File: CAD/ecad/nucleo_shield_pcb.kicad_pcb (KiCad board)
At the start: 2 copper layers, 70 x 57 mm, 6 parts, among them J1 CN7, J2 CN10

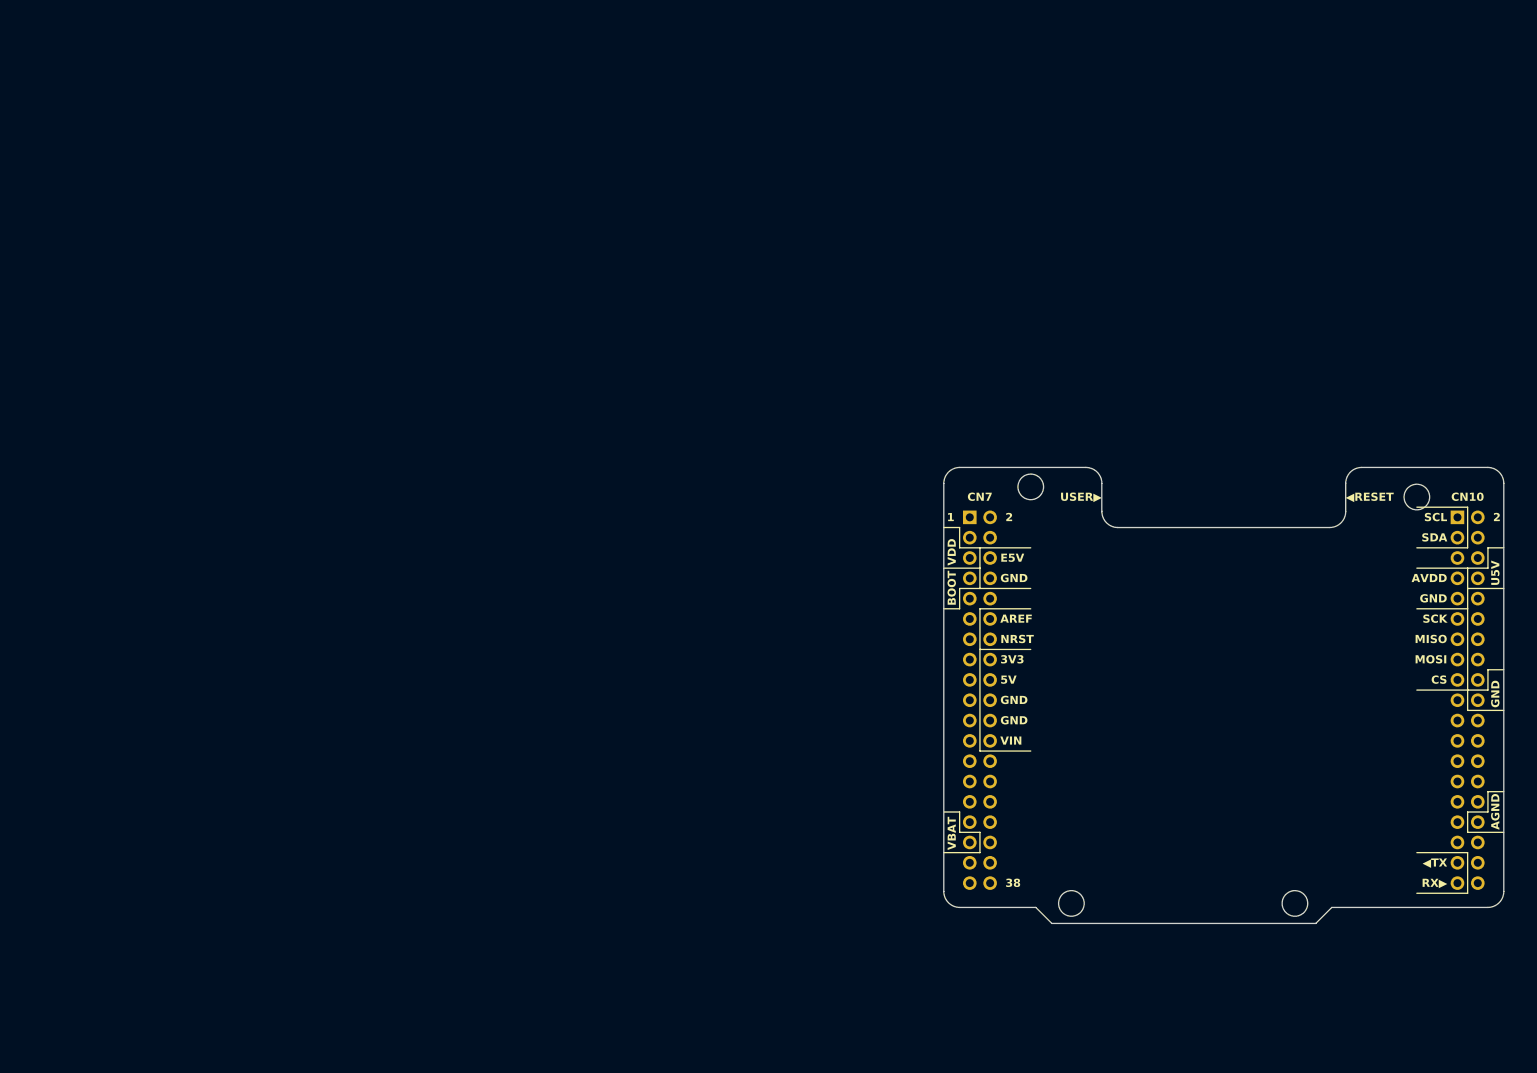
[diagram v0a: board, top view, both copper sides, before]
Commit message: Update KiCad schematic and layout with new ESP32 button circuitry
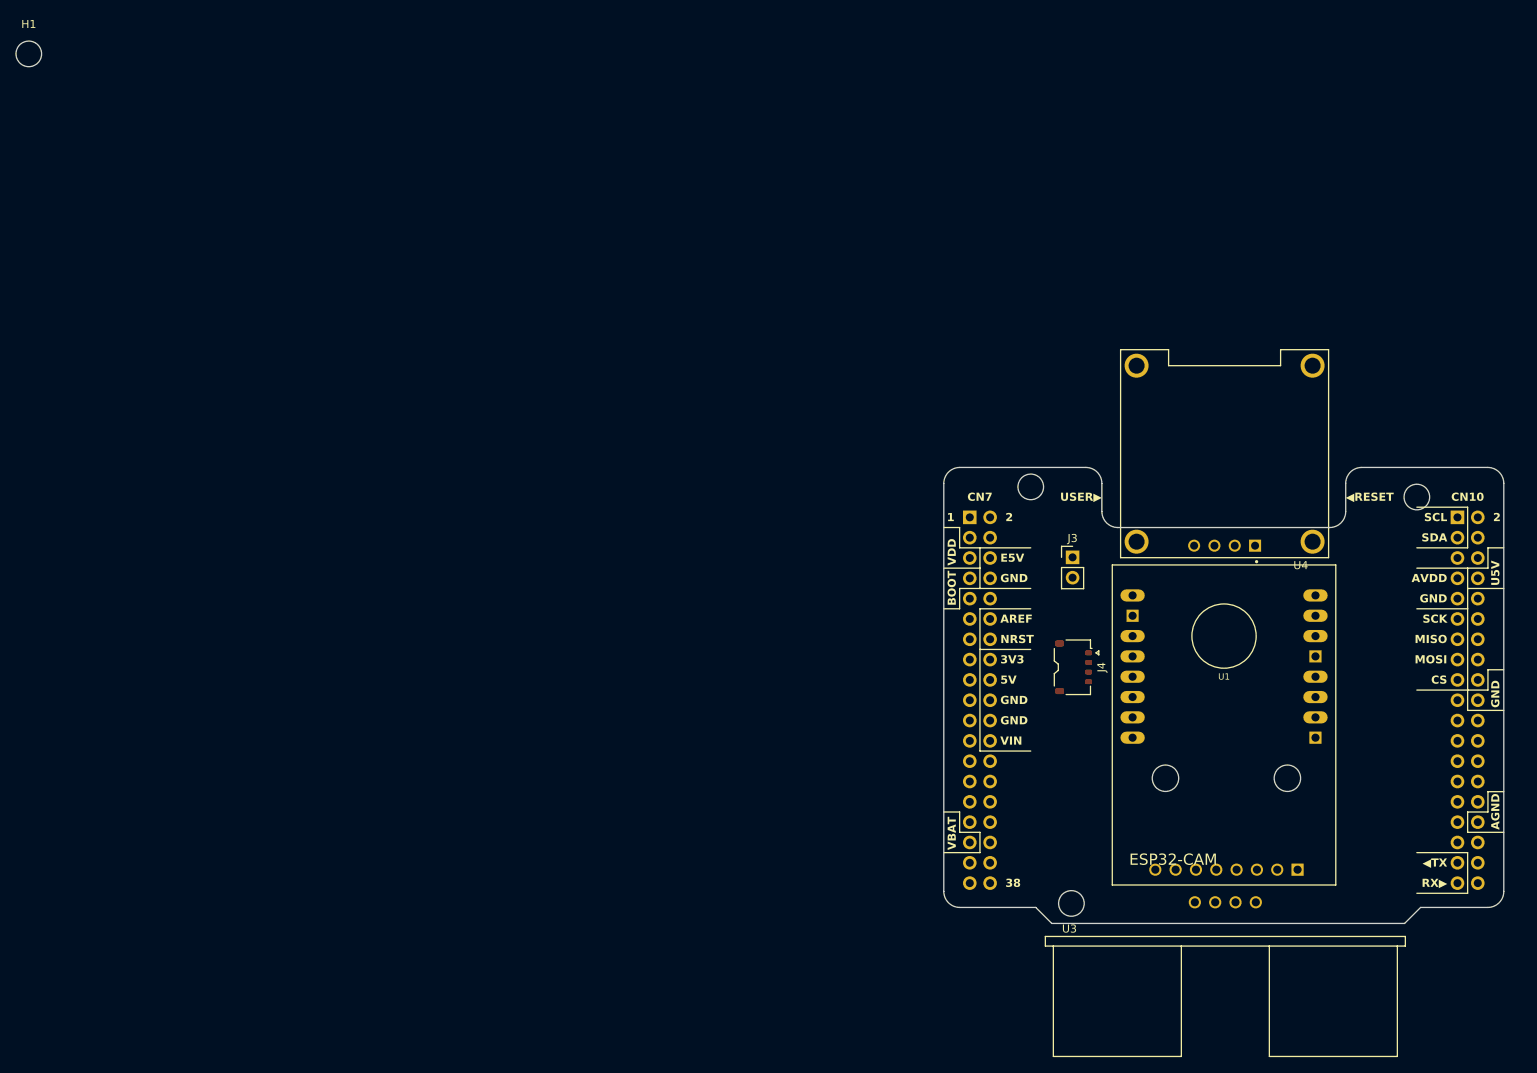
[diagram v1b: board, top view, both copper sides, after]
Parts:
- added J3: Conn_01x02_Pin, Connector_PinHeader_2.54mm:PinHeader_1x02_P2.54mm_Vertical, F.Cu at (133.5, 66.0)
- added J4: Conn_01x04_Socket, Connector_JST:JST_ACH_BM04B-ACHSS-A-GAN-ETF_1x04-1MP_P1.20mm_Vertical, F.Cu at (133.6, 79.7)
- added U1: ESP32-CAM, components:ESP32-CAM, F.Cu at (152.4, 80.9)
- added U2: ADXL345, components:MODULE_SEN-09836, B.Cu at (152.7, 98.7)
- added U3: HC-SR04, components:XCVR_HC-SR04, F.Cu at (152.6, 109.1)
- added U4: DM-OLED096-636, components:MODULE_DM-OLED096-636, F.Cu at (152.5, 53.0)
- moved H1 190.6 mm to (3.02, 3.02)
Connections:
- J2 pad 17: unconnected-(J2-Pin_17-Pad17) -> /tx/rx
- J2 pad 2: unconnected-(J2-Pin_2-Pad2) -> Net-(J2-Pin_2)
- J2 pad 33: unconnected-(J2-Pin_33-Pad33) -> /rx/tx
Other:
- outline, holes or cut-outs redrawn

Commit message: Fix component footprint libraries and resolve button shield pin mapping errors
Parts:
- removed H1: MountingHole, MountingHole:MountingHole_3.2mm_M3_ISO14580
- added D2: 1N4148, Diode_THT:D_DO-35_SOD27_P7.62mm_Horizontal, F.Cu at (175.8, 89.5)
- added SW1: CK_KMS2xxGP, Button_Switch_SMD:SW_SPST_PTS645Sx43SMTR92, F.Cu at (132.3, 97.0)
- added SW2: CK_KMS2xxGP, Button_Switch_SMD:SW_SPST_PTS645Sx43SMTR92, F.Cu at (172.0, 97.0)
- added SW3: CK_KMS2xxGP, Button_Switch_SMD:SW_SPST_PTS645Sx43SMTR92, F.Cu at (171.4, 68.9)
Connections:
- J1 pad 23: unconnected-(J1-Pin_23-Pad23) -> Net-(J1-Pin_23)
- J2 pad 19: unconnected-(J2-Pin_19-Pad19) -> Net-(J2-Pin_19)
- J2 pad 23: unconnected-(J2-Pin_23-Pad23) -> Net-(J2-Pin_23)
- J2 pad 3: unconnected-(J2-Pin_3-Pad3) -> /SCL
- J2 pad 5: unconnected-(J2-Pin_5-Pad5) -> /SDA
- U1 pad P$1: unconnected-(U1-GND@1-PadP$1) -> /reset
- U1 pad P$13: unconnected-(U1-GPIO15-PadP$13) -> Net-(U1-GPIO15)
- U2 pad 3: unconnected-(U2-CS-Pad3) -> +3V3
- U2 pad 6: unconnected-(U2-SDO-Pad6) -> GNDD
- U3 pad 2: unconnected-(U3-TRIG-Pad2) -> Net-(J2-Pin_23)
- U3 pad 3: unconnected-(U3-ECHO-Pad3) -> Net-(J2-Pin_19)
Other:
- board text added: "Controll Button"
- board text added: "LED FLASH"
- board text added: "RESET"

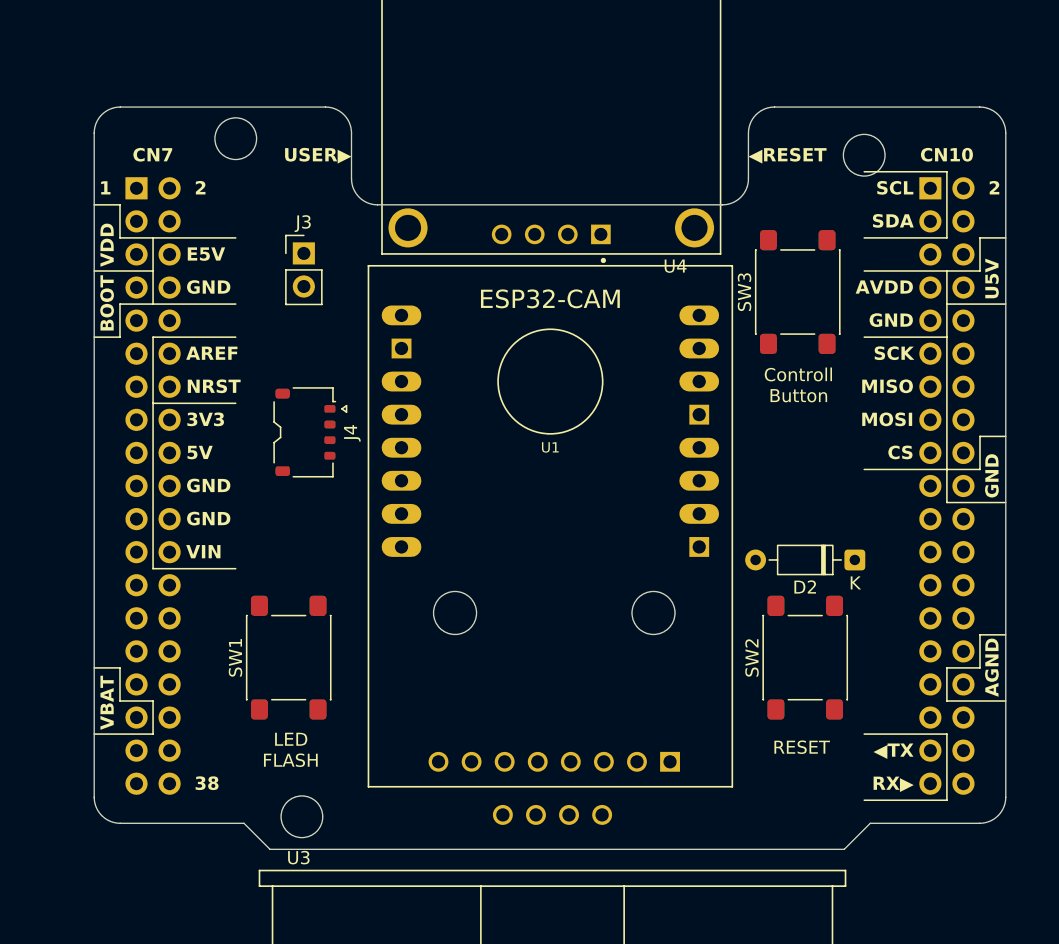
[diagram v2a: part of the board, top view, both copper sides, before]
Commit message: Update PCB and schematic: wire sensors, motor driver connector, and buttons
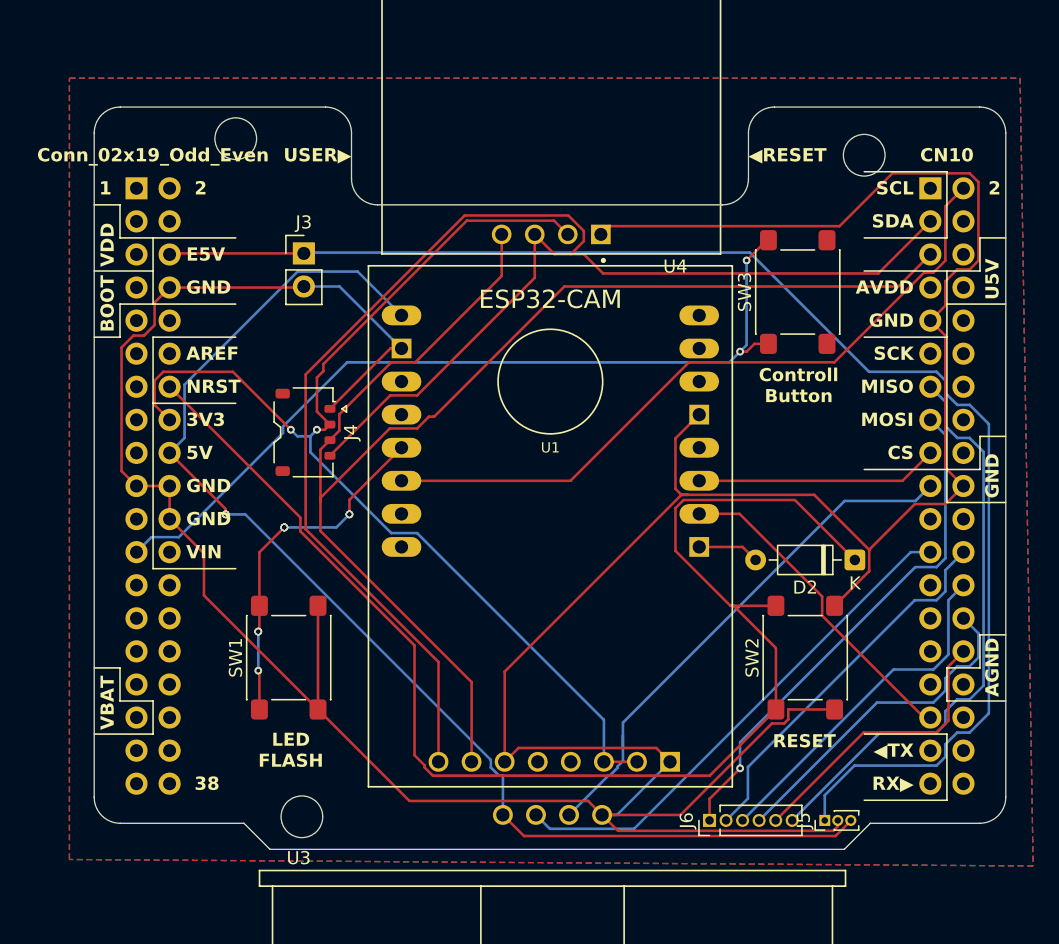
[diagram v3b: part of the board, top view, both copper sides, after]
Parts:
- added J5: Conn_01x03_Pin, Connector_PinHeader_1.00mm:PinHeader_1x03_P1.00mm_Vertical, F.Cu at (173.5, 109.5)
- added J6: Conn_01x06_Pin, Connector_PinHeader_1.27mm:PinHeader_1x06_P1.27mm_Vertical, F.Cu at (164.7, 109.5)
- J1: value CN7 -> Conn_02x19_Odd_Even
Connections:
- J2 pad 13: unconnected-(J2-Pin_13-Pad13) -> Net-(J2-Pin_13)
- J2 pad 15: unconnected-(J2-Pin_15-Pad15) -> Net-(J2-Pin_15)
- J2 pad 24: unconnected-(J2-Pin_24-Pad24) -> Net-(J2-Pin_24)
- J2 pad 26: unconnected-(J2-Pin_26-Pad26) -> Net-(J2-Pin_26)
- J2 pad 28: unconnected-(J2-Pin_28-Pad28) -> Net-(J2-Pin_28)
- J2 pad 30: unconnected-(J2-Pin_30-Pad30) -> Net-(J2-Pin_30)
- J4 pad MP: (no net) -> GNDD
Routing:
- net GNDD: track 0.00 -> 286.2 mm
- net /SCL: track 0.00 -> 121.1 mm
- net E5V: track 0.00 -> 108.9 mm
- net /SDA: track 0.00 -> 107.1 mm
- net RESET: track 0.00 -> 104.7 mm
- net +5V: track 0.00 -> 94.7 mm, vias 0 -> 3
- net +3V3: track 0.00 -> 86.7 mm, vias 0 -> 2
- net Net-(J1-Pin_23): track 0.00 -> 65.0 mm, vias 0 -> 2
- net Net-(J2-Pin_2): track 0.00 -> 54.9 mm
- net Net-(J2-Pin_13): track 0.00 -> 44.7 mm
- net Net-(J2-Pin_19): track 0.00 -> 40.9 mm
- net Net-(J2-Pin_15): track 0.00 -> 39.7 mm, vias 0 -> 1
- net Net-(J2-Pin_23): track 0.00 -> 39.5 mm
- net Net-(J2-Pin_24): track 0.00 -> 29.1 mm
- net Net-(U1-GPIO15): track 0.00 -> 27.0 mm, vias 0 -> 8
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- added copper zone on B.Cu, net GNDD
- added copper zone on F.Cu, net GNDD

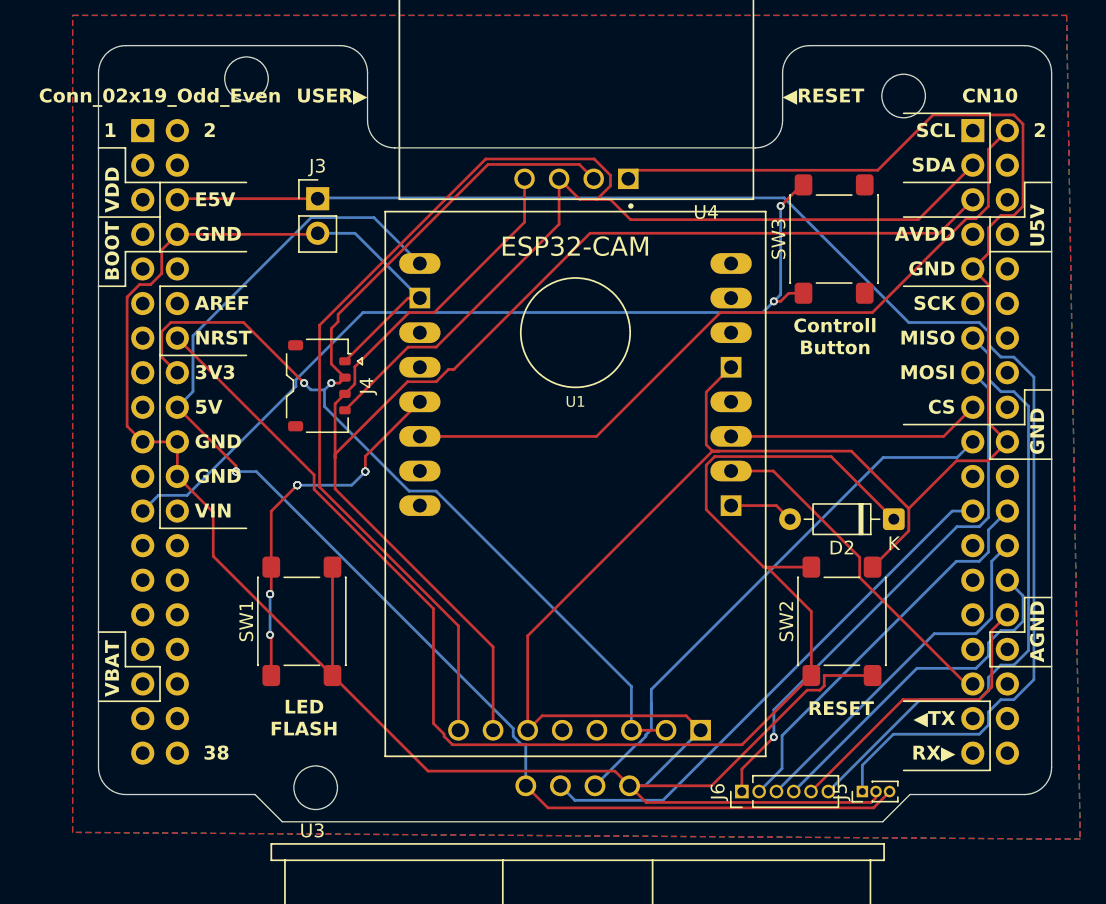
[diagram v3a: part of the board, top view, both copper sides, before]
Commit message: Add Mimir logo to PCB and update layout
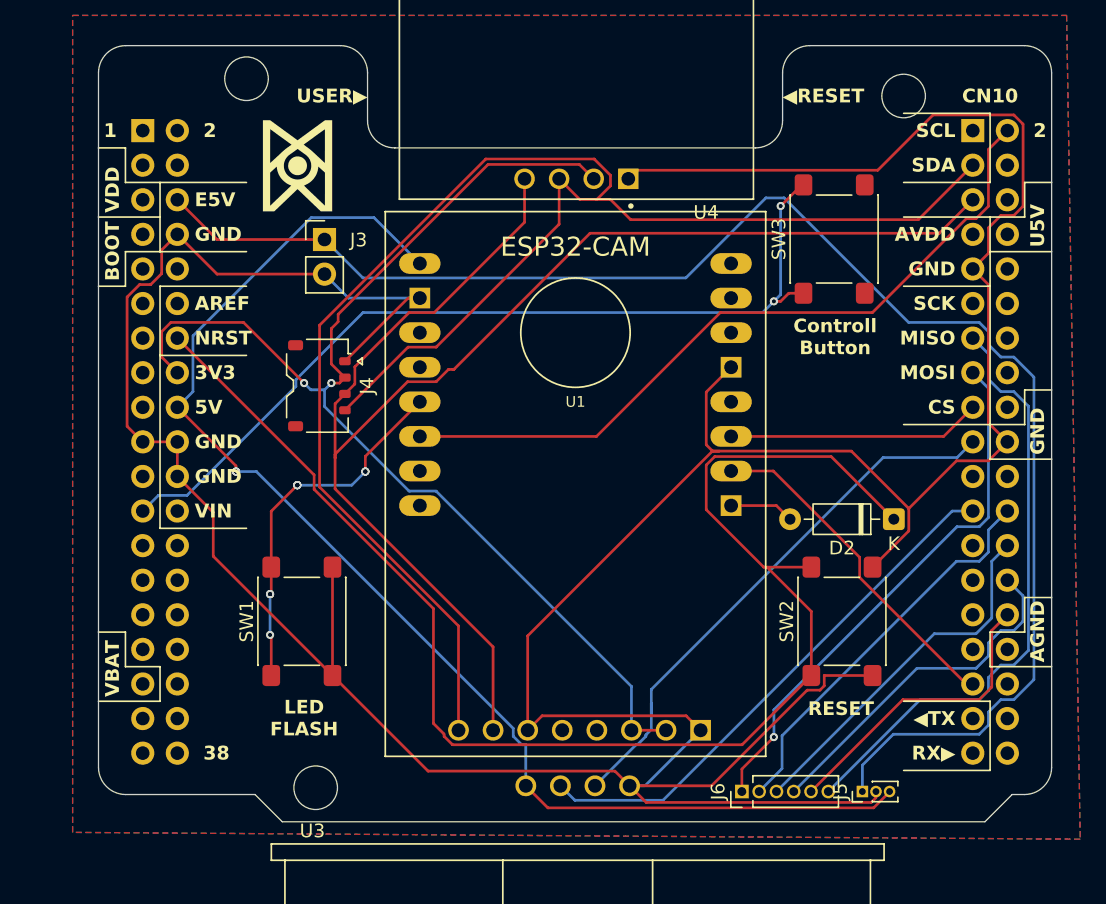
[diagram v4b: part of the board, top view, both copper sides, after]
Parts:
- added G***: LOGO, components:mimir, F.Cu at (132.0, 63.5)
- added REF**: OSHW-Symbol_13.4x12mm_SilkScreen, Symbol:OSHW-Symbol_13.4x12mm_SilkScreen, B.Cu at (152.5, 75.0)
- moved J3 3.04 mm to (134.0, 69.0)
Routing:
- net E5V: track 108.9 -> 113.8 mm
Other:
- outline, holes or cut-outs redrawn
